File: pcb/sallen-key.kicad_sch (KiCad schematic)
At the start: 27 parts

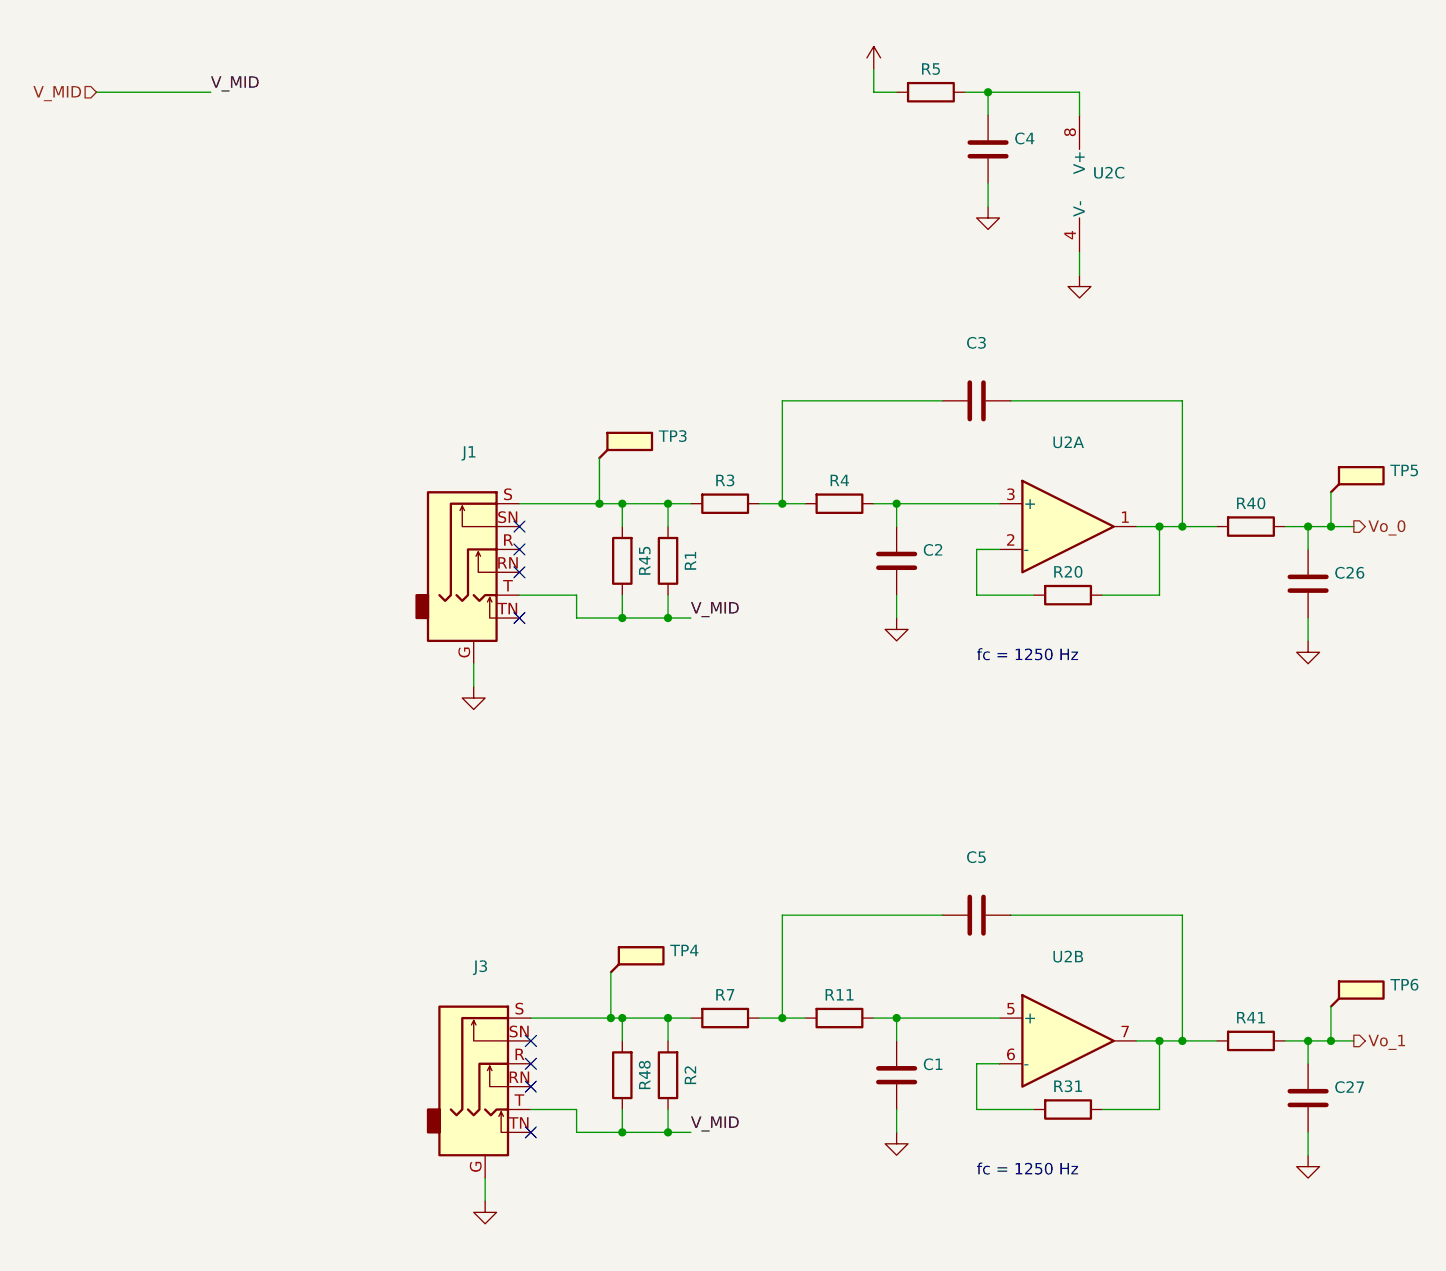
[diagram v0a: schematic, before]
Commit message: * Start replicating emonLibCM functionality
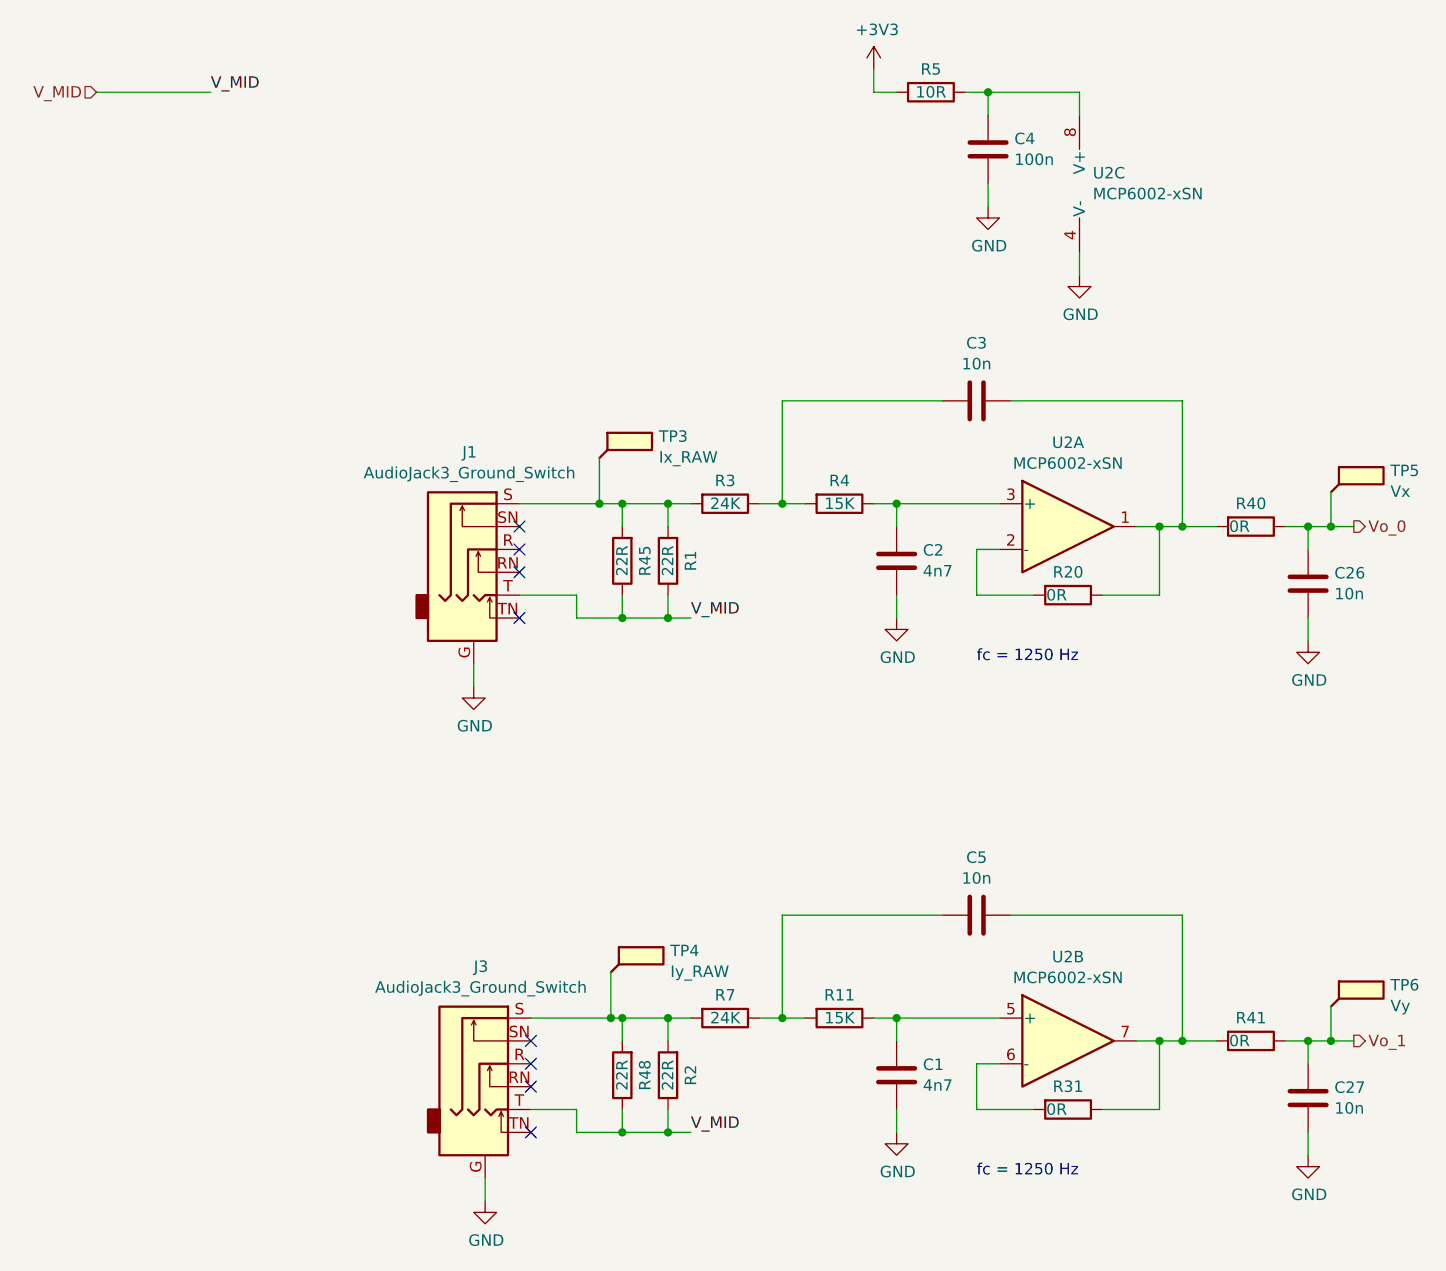
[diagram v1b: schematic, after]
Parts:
- C1, C2: value (none) -> 4n7; footprint (none) -> Capacitor_SMD:C_0805_2012Metric_Pad1.18x1.45mm_HandSolder
- C26, C27, C3, C5: value (none) -> 10n; footprint (none) -> Capacitor_SMD:C_0805_2012Metric_Pad1.18x1.45mm_HandSolder
- C4: value (none) -> 100n; footprint (none) -> Capacitor_SMD:C_0805_2012Metric_Pad1.18x1.45mm_HandSolder
- J1, J3: value (none) -> AudioJack3_Ground_Switch; footprint (none) -> Connector_Audio:Jack_3.5mm_CUI_SJ1-3535NG_Horizontal
- R1, R2, R45, R48: value (none) -> 22R; footprint (none) -> Resistor_SMD:R_0805_2012Metric_Pad1.20x1.40mm_HandSolder
- R11, R4: value (none) -> 15K; footprint (none) -> Resistor_SMD:R_0805_2012Metric_Pad1.20x1.40mm_HandSolder
- R20, R31, R40, R41: value (none) -> 0R; footprint (none) -> Resistor_SMD:R_0805_2012Metric_Pad1.20x1.40mm_HandSolder
- R3, R7: value (none) -> 24K; footprint (none) -> Resistor_SMD:R_0805_2012Metric_Pad1.20x1.40mm_HandSolder
- R5: value (none) -> 10R; footprint (none) -> Resistor_SMD:R_0805_2012Metric_Pad1.20x1.40mm_HandSolder
- TP3: value (none) -> Ix_RAW; footprint (none) -> TestPoint:TestPoint_THTPad_1.5x1.5mm_Drill0.7mm
- TP4: value (none) -> Iy_RAW; footprint (none) -> TestPoint:TestPoint_THTPad_1.5x1.5mm_Drill0.7mm
- TP5: value (none) -> Vx; footprint (none) -> TestPoint:TestPoint_THTPad_1.5x1.5mm_Drill0.7mm
- TP6: value (none) -> Vy; footprint (none) -> TestPoint:TestPoint_THTPad_1.5x1.5mm_Drill0.7mm
- U2: value (none) -> MCP6002-xSN; footprint (none) -> Package_SO:SOIC-8_3.9x4.9mm_P1.27mm
